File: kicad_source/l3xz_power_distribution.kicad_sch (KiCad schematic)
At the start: 16 parts, among them J1 PowerPole_ver, J2 PowerPole_ver, J3 PowerPole_ver, J4 PowerPole_ver, J5 PowerPole_ver, J6 PowerPole_ver, J7 PowerPole_ver, J8 PowerPole_ver

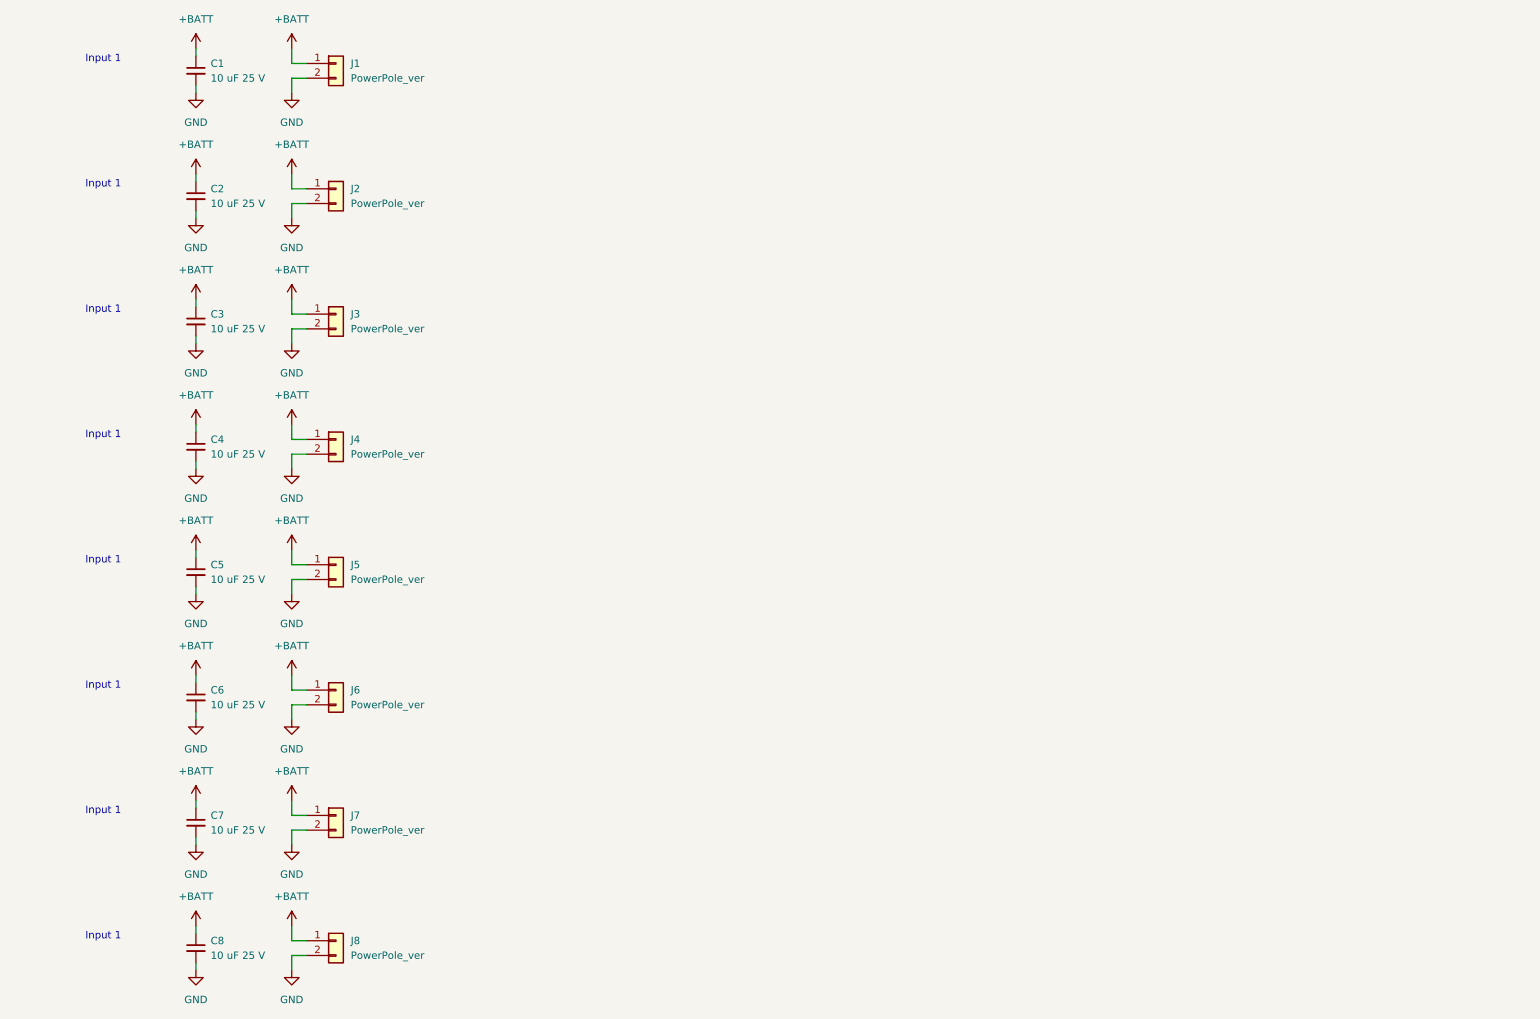
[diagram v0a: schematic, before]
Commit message: added 4 more power poles
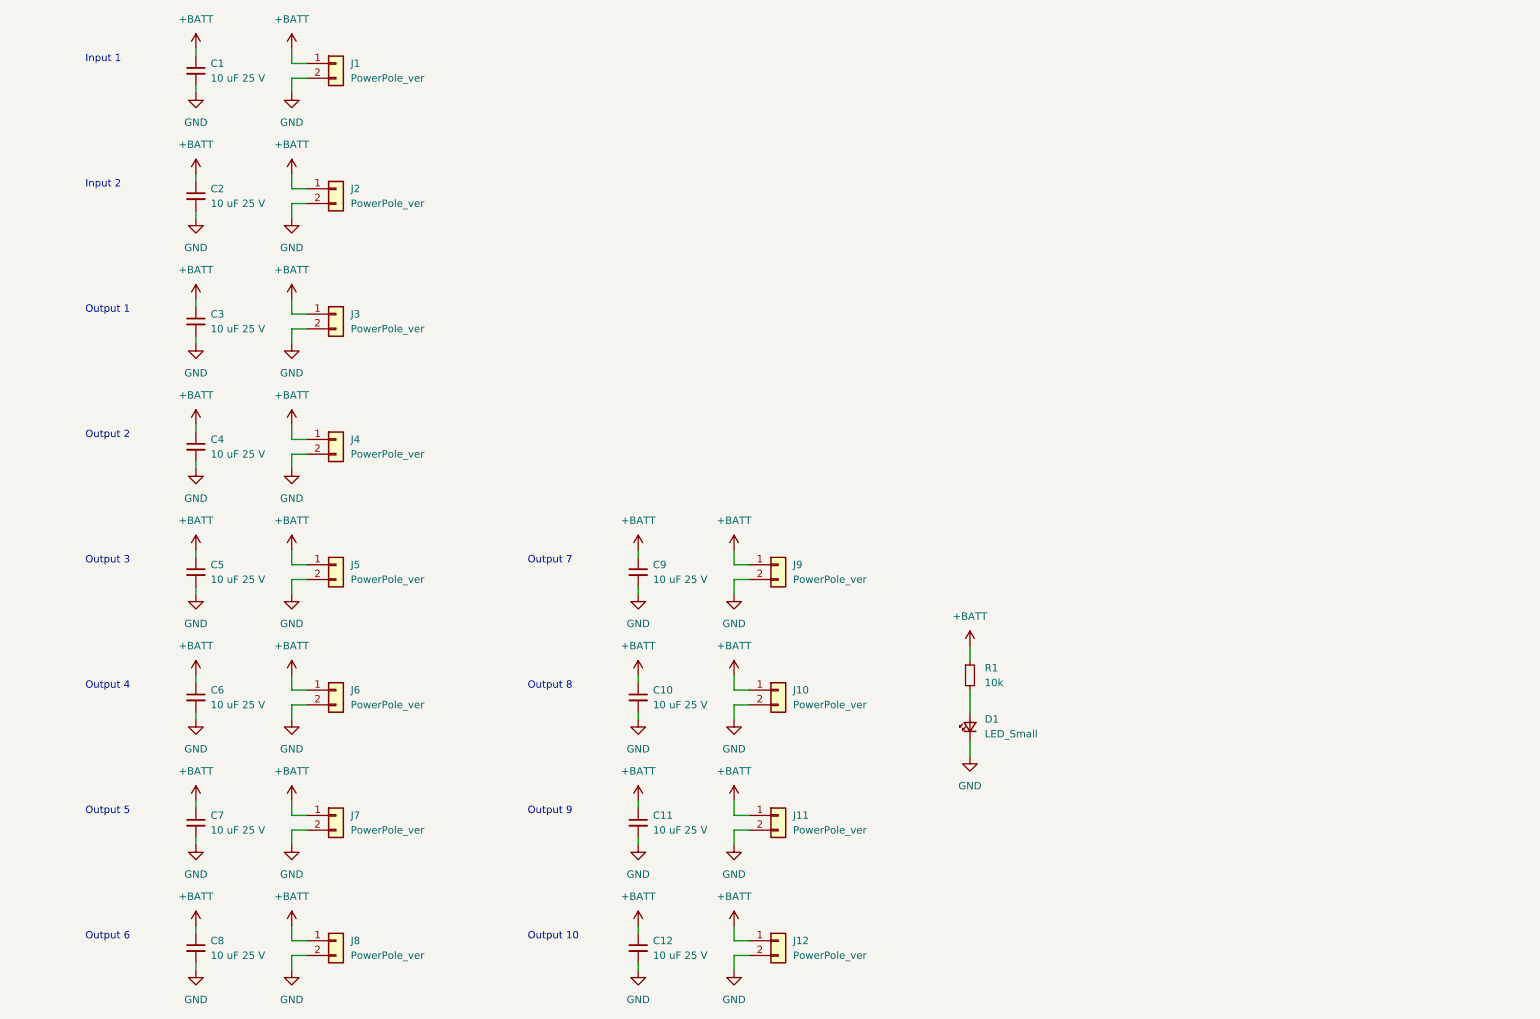
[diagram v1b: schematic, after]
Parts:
- added C10, C11, C12, C9: 10 uF 25 V, Capacitor_SMD:C_1210_3225Metric, symbol Device:C_Small
- added D1: LED_Small, LED_SMD:LED_0603_1608Metric, symbol Device:LED_Small
- added J10, J11, J12, J9: PowerPole_ver, generationmake:POWERPOLE_2, symbol Connector_Generic:Conn_01x02
- added R1: 10k, Resistor_SMD:R_0603_1608Metric, symbol Device:R_Small
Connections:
- net +BATT: now also C10.1, C11.1, C12.1, C9.1, J10.1 (Pin_1), J11.1 (Pin_1), J12.1 (Pin_1), J9.1 (Pin_1), R1.1
- net GND: now also C10.2, C11.2, C12.2, C9.2, D1.1 (K), J10.2 (Pin_2), J11.2 (Pin_2), J12.2 (Pin_2), J9.2 (Pin_2)
- new net: D1.2 (A), R1.2
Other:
- note added: "Input 2"
- note added: "Output 1"
- note added: "Output 10"
- note added: "Output 2"
- note added: "Output 3"
- note added: "Output 4"
- note added: "Output 5"
- note added: "Output 6"
- note added: "Output 7"
- note added: "Output 8"
- note added: "Output 9"

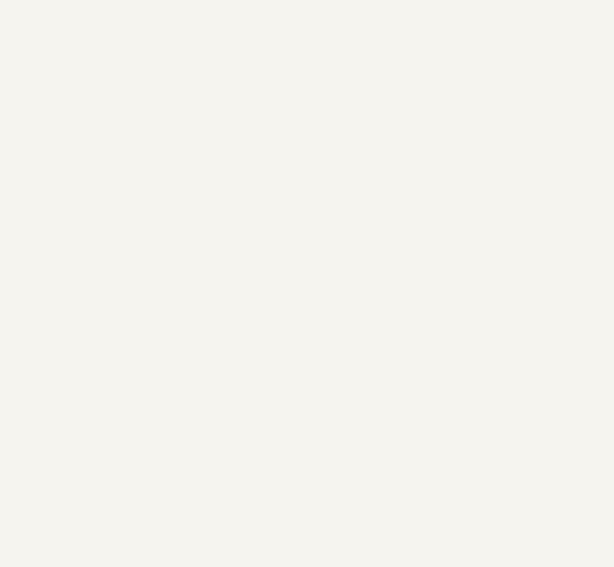
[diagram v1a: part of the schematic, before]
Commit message: added some labels
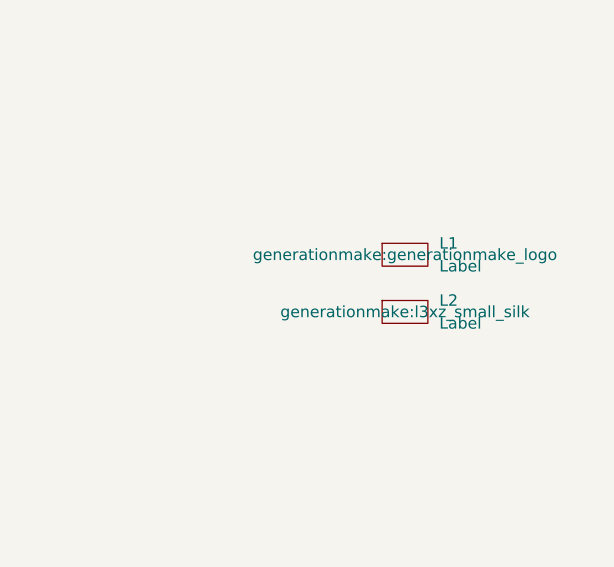
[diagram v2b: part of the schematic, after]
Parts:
- added L1: Label, generationmake:generationmake_logo, symbol generationmake:Label
- added L2: Label, generationmake:l3xz_small_silk, symbol generationmake:Label
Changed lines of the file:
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@@
     (pin "1")
+  )
+  (symbol (lib_id "generationmake:Label") (at 257.81 151.13 0) (unit 1)
+    (in_bom yes) (on_board yes) (fields_autoplaced)
+    (property "Reference" "L1" (id 0) (at 261.62 149.8599 0)
+      (effects (font (size 1.27 1.27)) (justify left))
+    )
+    (property "Value" "Label" (id 1) (at 261.62 152.3999 0)
+      (effects (font (size 1.27 1.27)) (justify left))
+    )
+    (property "Footprint" "generationmake:generationmake_logo" (id 2) (at 257.81 151.13 0))
+    (property "Datasheet" "" (id 3) (at 257.81 151.13 0)
+      (effects (font (size 1.27 1.27)) hide)
+    )
   )
   (symbol (lib_id "Device:C_Small") (at 49.53 92.71 0) (unit 1)
@@
     )
     (pin "1")
+  )
+  (symbol (lib_id "generationmake:Label") (at 257.81 157.48 0) (unit 1)
+    (in_bom yes) (on_board yes) (fields_autoplaced)
+    (property "Reference" "L2" (id 0) (at 261.62 156.2099 0)
+      (effects (font (size 1.27 1.27)) (justify left))
+    )
+    (property "Value" "Label" (id 1) (at 261.62 158.7499 0)
+      (effects (font (size 1.27 1.27)) (justify left))
+    )
+    (property "Footprint" "generationmake:l3xz_small_silk" (id 2) (at 257.81 157.48 0))
+    (property "Datasheet" "" (id 3) (at 257.81 157.48 0)
+      (effects (font (size 1.27 1.27)) hide)
+    )
   )
   (symbol (lib_id "power:+BATT") (at 66.04 45.72 0) (unit 1)
@@
       (reference "J12") (unit 1) (value "PowerPole_ver") (footprint "generationmake:POWERPOLE_2")
     )
+    (path "/a1950903-4a3c-46b5-ac02-34174b3e58a9"
+      (reference "L1") (unit 1) (value "Label") (footprint "generationmake:generationmake_logo")
+    )
+    (path "/cb6499cb-9c1c-4bfd-9c22-1a0779cd54ab"
+      (reference "L2") (unit 1) (value "Label") (footprint "generationmake:l3xz_small_silk")
+    )
     (path "/5a85479c-fca6-4da9-9ced-dadc3e18f6c4"

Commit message: moved to horizontal power poles
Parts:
- J1, J10, J11, J12, J2, J3, J4, J5, J6, J7, J8, J9: footprint generationmake:POWERPOLE_2 -> generationmake:POWERPOLE_hor90_2
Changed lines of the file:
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@@
   (title_block
     (title "l3xz_power_distribution")
-    (date "2023-03-29")
+    (date "2023-04-08")
     (rev "0.1")
     (company "107-systems")
@@
       (effects (font (size 1.27 1.27)) (justify left))
     )
-    (property "Footprint" "generationmake:POWERPOLE_2" (id 2) (at 73.66 177.8 0)
+    (property "Footprint" "generationmake:POWERPOLE_hor90_2" (id 2) (at 73.66 177.8 0)
       (effects (font (size 1.27 1.27)) hide)
     )
@@
       (effects (font (size 1.27 1.27)) (justify left))
     )
-    (property "Footprint" "generationmake:POWERPOLE_2" (id 2) (at 73.66 69.85 0)
+    (property "Footprint" "generationmake:POWERPOLE_hor90_2" (id 2) (at 73.66 69.85 0)
       (effects (font (size 1.27 1.27)) hide)
     )
@@
       (effects (font (size 1.27 1.27)) (justify left))
     )
-    (property "Footprint" "generationmake:POWERPOLE_2" (id 2) (at 73.66 91.44 0)
+    (property "Footprint" "generationmake:POWERPOLE_hor90_2" (id 2) (at 73.66 91.44 0)
       (effects (font (size 1.27 1.27)) hide)
     )
@@
       (effects (font (size 1.27 1.27)) (justify left))
     )
-    (property "Footprint" "generationmake:POWERPOLE_2" (id 2) (at 73.66 26.67 0)
+    (property "Footprint" "generationmake:POWERPOLE_hor90_2" (id 2) (at 73.66 26.67 0)
       (effects (font (size 1.27 1.27)) hide)
     )
@@
       (effects (font (size 1.27 1.27)) (justify left))
     )
-    (property "Footprint" "generationmake:POWERPOLE_2" (id 2) (at 73.66 113.03 0)
+    (property "Footprint" "generationmake:POWERPOLE_hor90_2" (id 2) (at 73.66 113.03 0)
       (effects (font (size 1.27 1.27)) hide)
     )
@@
       (effects (font (size 1.27 1.27)) (justify left))
     )
-    (property "Footprint" "generationmake:POWERPOLE_2" (id 2) (at 73.66 48.26 0)
+    (property "Footprint" "generationmake:POWERPOLE_hor90_2" (id 2) (at 73.66 48.26 0)
       (effects (font (size 1.27 1.27)) hide)
     )
@@
       (effects (font (size 1.27 1.27)) (justify left))
     )
-    (property "Footprint" "generationmake:POWERPOLE_2" (id 2) (at 73.66 134.62 0)
+    (property "Footprint" "generationmake:POWERPOLE_hor90_2" (id 2) (at 73.66 134.62 0)
       (effects (font (size 1.27 1.27)) hide)
     )
@@
       (effects (font (size 1.27 1.27)) (justify left))
     )
-    (property "Footprint" "generationmake:POWERPOLE_2" (id 2) (at 73.66 156.21 0)
+    (property "Footprint" "generationmake:POWERPOLE_hor90_2" (id 2) (at 73.66 156.21 0)
       (effects (font (size 1.27 1.27)) hide)
     )
@@
       (effects (font (size 1.27 1.27)) (justify left))
     )
-    (property "Footprint" "generationmake:POWERPOLE_2" (id 2) (at 149.86 134.62 0)
+    (property "Footprint" "generationmake:POWERPOLE_hor90_2" (id 2) (at 149.86 134.62 0)
       (effects (font (size 1.27 1.27)) hide)
     )
@@
       (effects (font (size 1.27 1.27)) (justify left))
     )
-    (property "Footprint" "generationmake:POWERPOLE_2" (id 2) (at 149.86 113.03 0)
+    (property "Footprint" "generationmake:POWERPOLE_hor90_2" (id 2) (at 149.86 113.03 0)
       (effects (font (size 1.27 1.27)) hide)
     )
@@
       (effects (font (size 1.27 1.27)) (justify left))
     )
-    (property "Footprint" "generationmake:POWERPOLE_2" (id 2) (at 149.86 156.21 0)
+    (property "Footprint" "generationmake:POWERPOLE_hor90_2" (id 2) (at 149.86 156.21 0)
       (effects (font (size 1.27 1.27)) hide)
     )
@@
       (effects (font (size 1.27 1.27)) (justify left))
     )
-    (property "Footprint" "generationmake:POWERPOLE_2" (id 2) (at 149.86 177.8 0)
+    (property "Footprint" "generationmake:POWERPOLE_hor90_2" (id 2) (at 149.86 177.8 0)
       (effects (font (size 1.27 1.27)) hide)
     )
@@
     )
     (path "/40ba9434-20aa-4351-8c1b-12ceb107b778"
-      (reference "J1") (unit 1) (value "PowerPole_ver") (footprint "generationmake:POWERPOLE_2")
+      (reference "J1") (unit 1) (value "PowerPole_ver") (footprint "generationmake:POWERPOLE_hor90_2")
     )
     (path "/56ac6ee4-51a7-4448-96d6-6cee7f6e5180"
-      (reference "J2") (unit 1) (value "PowerPole_ver") (footprint "generationmake:POWERPOLE_2")
+      (reference "J2") (unit 1) (value "PowerPole_ver") (footprint "generationmake:POWERPOLE_hor90_2")
     )
     (path "/14fa66c4-a2f8-470c-9fa0-7ef33a3799b9"
-      (reference "J3") (unit 1) (value "PowerPole_ver") (footprint "generationmake:POWERPOLE_2")
+      (reference "J3") (unit 1) (value "PowerPole_ver") (footprint "generationmake:POWERPOLE_hor90_2")
     )
     (path "/2a0b43ef-a9ce-40fc-a96e-e3c13483815c"
-      (reference "J4") (unit 1) (value "PowerPole_ver") (footprint "generationmake:POWERPOLE_2")
+      (reference "J4") (unit 1) (value "PowerPole_ver") (footprint "generationmake:POWERPOLE_hor90_2")
     )
     (path "/4de92e2d-e5a2-4990-b923-21f393e201e1"
-      (reference "J5") (unit 1) (value "PowerPole_ver") (footprint "generationmake:POWERPOLE_2")
+      (reference "J5") (unit 1) (value "PowerPole_ver") (footprint "generationmake:POWERPOLE_hor90_2")
     )
     (path "/67613e61-33cb-4822-a044-a39f013104c6"
-      (reference "J6") (unit 1) (value "PowerPole_ver") (footprint "generationmake:POWERPOLE_2")
+      (reference "J6") (unit 1) (value "PowerPole_ver") (footprint "generationmake:POWERPOLE_hor90_2")
     )
     (path "/8244a590-4142-48a4-bd21-17cb6ffc8d63"
-      (reference "J7") (unit 1) (value "PowerPole_ver") (footprint "generationmake:POWERPOLE_2")
+      (reference "J7") (unit 1) (value "PowerPole_ver") (footprint "generationmake:POWERPOLE_hor90_2")
     )
     (path "/0077bf59-4d8e-4ff2-8483-dc10b99daa43"
-      (reference "J8") (unit 1) (value "PowerPole_ver") (footprint "generationmake:POWERPOLE_2")
+      (reference "J8") (unit 1) (value "PowerPole_ver") (footprint "generationmake:POWERPOLE_hor90_2")
     )
     (path "/b9f305a9-46c5-41ea-939a-abd96169abc4"
-      (reference "J9") (unit 1) (value "PowerPole_ver") (footprint "generationmake:POWERPOLE_2")
+      (reference "J9") (unit 1) (value "PowerPole_ver") (footprint "generationmake:POWERPOLE_hor90_2")
     )
     (path "/a282b5cf-6262-4e6b-a4a8-fbf829091362"
-      (reference "J10") (unit 1) (value "PowerPole_ver") (footprint "generationmake:POWERPOLE_2")
+      (reference "J10") (unit 1) (value "PowerPole_ver") (footprint "generationmake:POWERPOLE_hor90_2")
     )
     (path "/bc9312a9-cbf3-4aea-85e3-2ab738ca19f8"
-      (reference "J11") (unit 1) (value "PowerPole_ver") (footprint "generationmake:POWERPOLE_2")
+      (reference "J11") (unit 1) (value "PowerPole_ver") (footprint "generationmake:POWERPOLE_hor90_2")
     )
     (path "/cad47cd4-1cdb-4f8f-a614-e67e4c053e60"
-      (reference "J12") (unit 1) (value "PowerPole_ver") (footprint "generationmake:POWERPOLE_2")
+      (reference "J12") (unit 1) (value "PowerPole_ver") (footprint "generationmake:POWERPOLE_hor90_2")
     )
     (path "/a1950903-4a3c-46b5-ac02-34174b3e58a9"
